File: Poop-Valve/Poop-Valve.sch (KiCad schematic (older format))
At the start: 51 parts, among them J1 RaspberryPi, J10 Valve Sig, J11 Conn_01x02_Male, J12 Relays, J13 LEDs, J14 24VDC, J15 Sensor, J16 Grove LCD, J2 Valve, J3 Charger, J4 Override, J5 Ovr Switch, J6 Power, J7 12VDC, J8 Conn_01x02_Male, J9 Conn_01x02_Male, K1 Override Relays, K2 Polarity Reverse, K3 Enable Relays, K4 Relay_Module, K5 Direction Relays, K6 Polarity Reverse, Q1 2N2222, Q2 2N2222, SW1 Override, SW2 Master Override, SW2 SW_DPDT_x2, SW3 Open/Close, U1 Opened, U2 Closed, U3 Override, U4 MCP3008

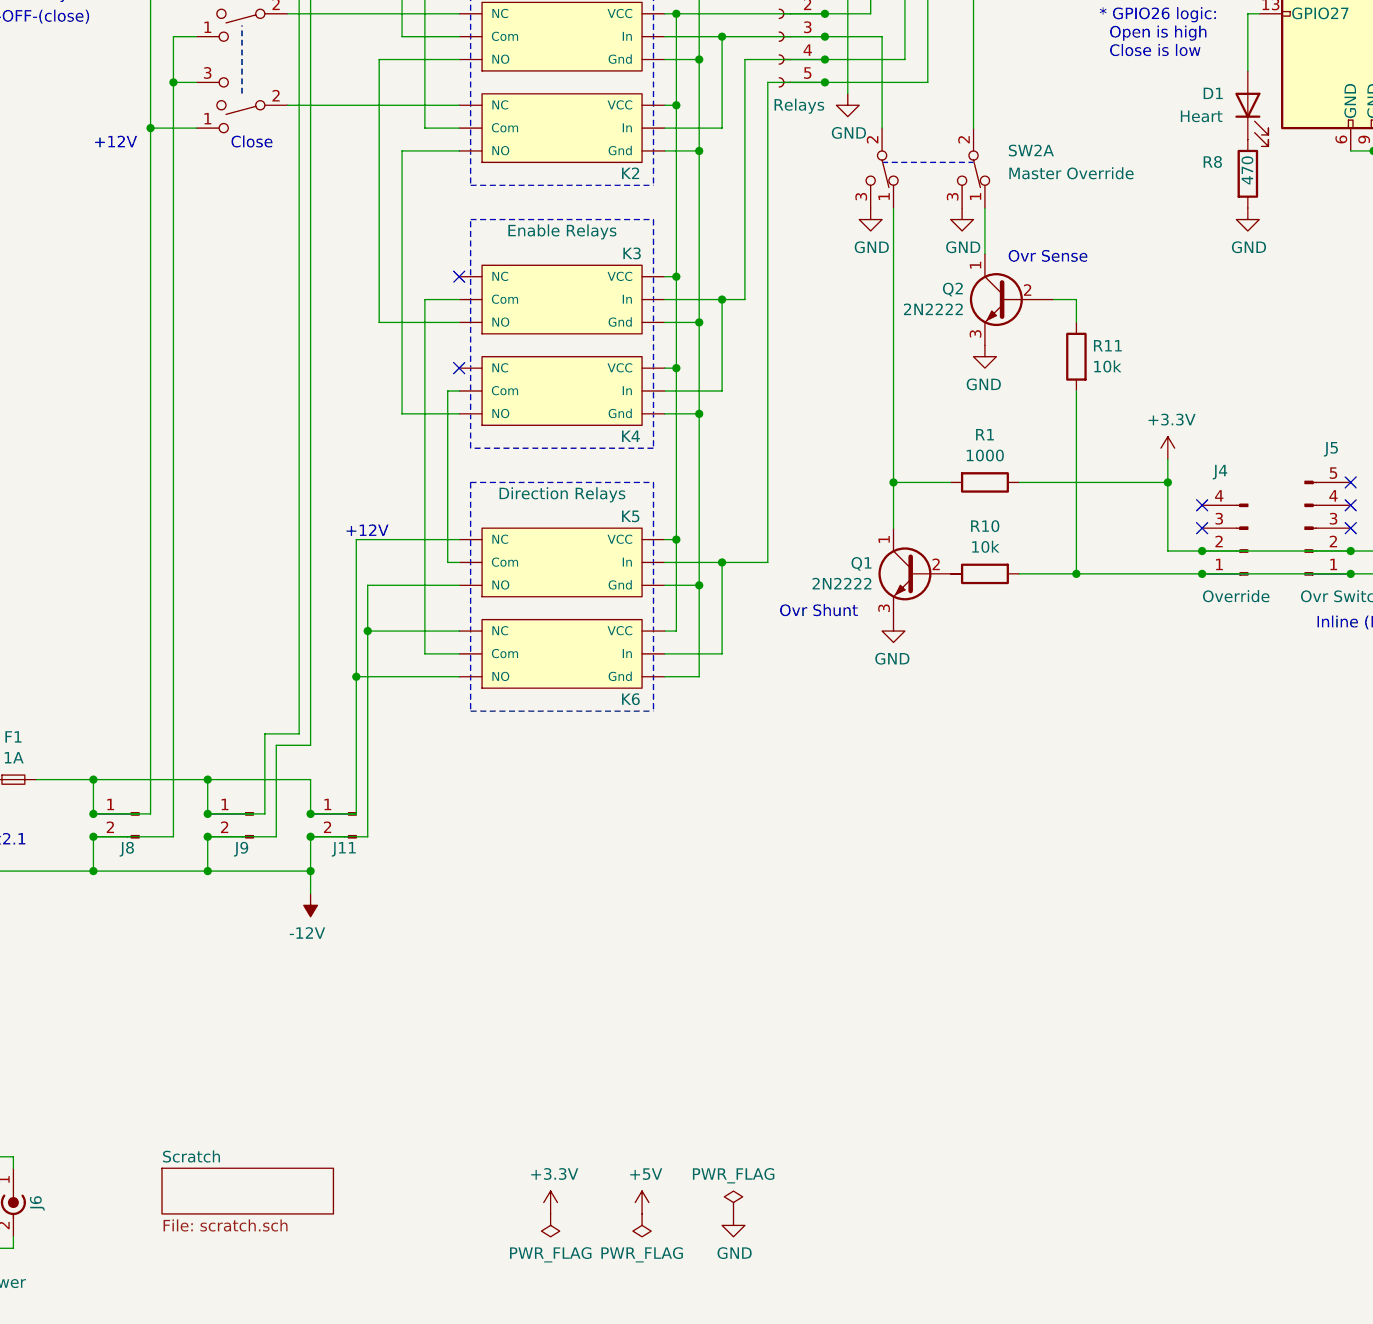
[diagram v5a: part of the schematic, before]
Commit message: v0.11 reconfigure 3.3v override relay drive
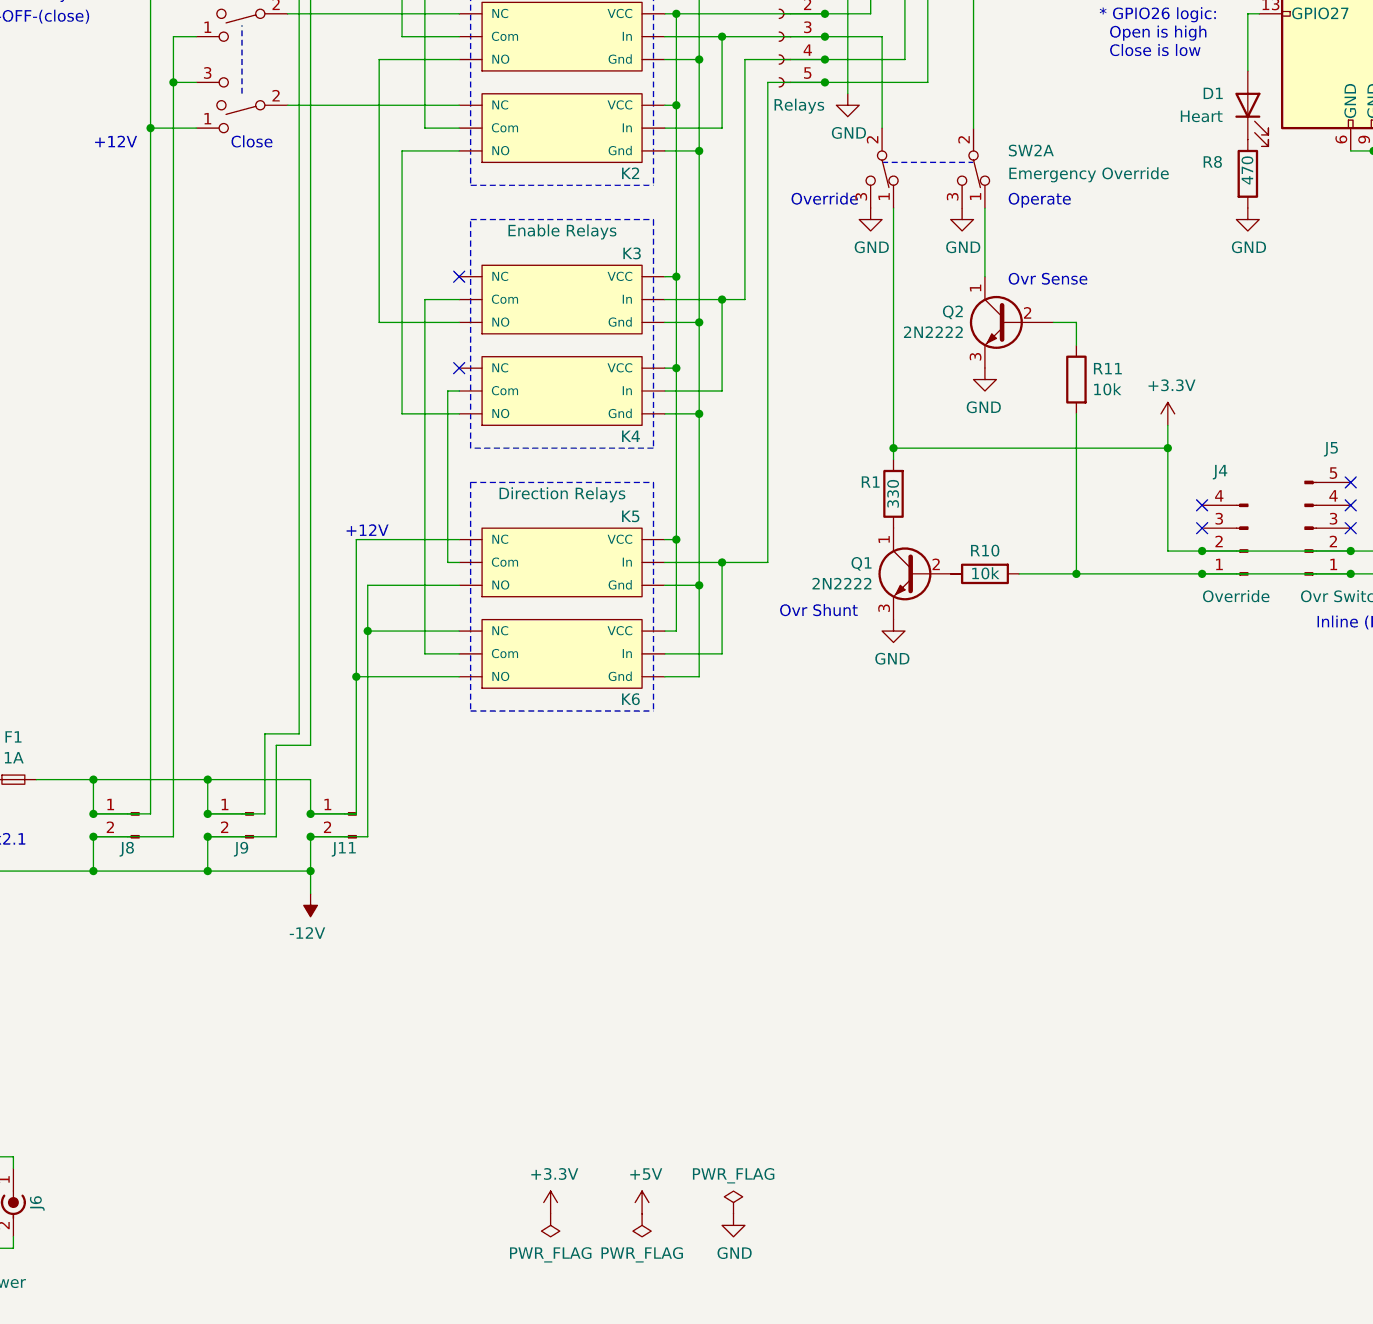
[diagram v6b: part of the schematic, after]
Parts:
- R1: value 1000 -> 330
- SW2: value Master Override -> Emergency Override
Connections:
- net +3V3: now also R1.2, SW?.1 (A); no longer R1.1
- new net: K1.~ (VCC), K2.~ (VCC), K3.~ (VCC), K4.~ (VCC), K5.~ (VCC), K6.~ (VCC)
- new net: K1.~ (VCC), K3.~ (VCC)
- new net: K3.~ (VCC), K6.~ (VCC)
- new net: K2.~ (VCC), K4.~ (VCC)
- new net: K4.~ (VCC), K5.~ (VCC)
- new net: Q1.1 (C), R1.1
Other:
- note added: "Operate"
- note added: "Override"
- moved on the sheet: Q2, R1, R11
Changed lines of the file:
@@
 $Descr USLetter 11000 8500
 encoding utf-8
-Sheet 1 2
+Sheet 1 1
 Title "Poop Valve Controller"
-Date "2023-02-01"
-Rev "0.10 (draft)"
+Date "2023-03-19"
+Rev "0.11 (draft)"
 Comp "Robert Ferguson Observatory"
-Comment1 "v0.7 correct ADC sample wiring"
-Comment2 "v0.8 reconfigure manual override; updated layout for clarity"
-Comment3 "v0.9 add override shunt and sense transistors "
-Comment4 "v0.10 add Master Override switch"
+Comment1 "v0.8 reconfigure manual override; updated layout for clarity"
+Comment2 "v0.9 add override shunt and sense transistors "
+Comment3 "v0.10 add Master Override switch"
+Comment4 "v0.11 reconfigure 3.3v override relay drive"
 $EndDescr
 $Comp
@@
 L power:+3.3V #PWR02
 U 1 1 64418208
-P 6450 5750
-F 0 "#PWR02" H 6450 5600 50  0001 C CNN
-F 1 "+3.3V" H 6465 5923 50  0000 C CNN
-F 2 "" H 6450 5750 50  0001 C CNN
-F 3 "" H 6450 5750 50  0001 C CNN
-	1    6450 5750
+P 6450 5600
+F 0 "#PWR02" H 6450 5450 50  0001 C CNN
+F 1 "+3.3V" H 6465 5773 50  0000 C CNN
+F 2 "" H 6450 5600 50  0001 C CNN
+F 3 "" H 6450 5600 50  0001 C CNN
+	1    6450 5600
 	1    0    0    -1
 $EndComp
@@
 Wire Wire Line
 	4950 3900 5200 3900
-$Sheet
-S 2050 8850 750  200
-U 65DFE627
-F0 "Scratch" 50
-F1 "scratch.sch" 50
-$EndSheet
 Wire Wire Line
 	2100 4100 2100 7400
@@
 AR Path="/65DFE627/6627A51F" Ref="R?"  Part="1"
 AR Path="/6627A51F" Ref="R10"  Part="1"
-F 0 "R10" V 5443 6250 50  0000 C CNN
-F 1 "10k" V 5534 6250 50  0000 C CNN
+F 0 "R10" V 5550 6250 50  0000 C CNN
+F 1 "10k" V 5650 6250 50  0000 C CNN
 F 2 "" V 5580 6250 50  0001 C CNN
 F 3 "~" H 5650 6250 50  0001 C CNN
@@
 	1    0    0    1
 $EndComp
-$Comp
-L Device:R R1
-U 1 1 664501BE
-P 5650 5850
-F 0 "R1" V 5443 5850 50  0000 C CNN
-F 1 "1000" V 5534 5850 50  0000 C CNN
-F 2 "" V 5580 5850 50  0001 C CNN
-F 3 "~" H 5650 5850 50  0001 C CNN
-	1    5650 5850
-	0    1    1    0
-$EndComp
 Wire Wire Line
 	5800 6250 6050 6250
-Wire Wire Line
-	6450 5750 6450 5850
 Wire Wire Line
 	6450 6150 6600 6150
 Text Notes 4750 6450 0    50   ~ 0
 Ovr Shunt
-Connection ~ 5250 5850
-Wire Wire Line
-	5250 5850 5250 6050
-Connection ~ 6450 5850
-Wire Wire Line
-	6450 5850 6450 6150
-Wire Wire Line
-	5800 5850 6450 5850
 $Comp
 L Device:R R?
 U 1 1 6659FCFC
-P 6050 5300
+P 6050 5400
 AR Path="/65DFE627/6659FCFC" Ref="R?"  Part="1"
 AR Path="/6659FCFC" Ref="R11"  Part="1"
-F 0 "R11" H 5980 5346 50  0000 R CNN
-F 1 "10k" H 5980 5255 50  0000 R CNN
-F 2 "" V 5980 5300 50  0001 C CNN
-F 3 "~" H 6050 5300 50  0001 C CNN
-	1    6050 5300
+F 0 "R11" H 5980 5446 50  0000 R CNN
+F 1 "10k" H 5980 5355 50  0000 R CNN
+F 2 "" V 5980 5400 50  0001 C CNN
+F 3 "~" H 6050 5400 50  0001 C CNN
+	1    6050 5400
 	-1   0    0    -1
 $EndComp
@@
 L power:GND #PWR?
 U 1 1 6659FD02
-P 5650 5250
+P 5650 5350
 AR Path="/65DFE627/6659FD02" Ref="#PWR?"  Part="1"
 AR Path="/6659FD02" Ref="#PWR022"  Part="1"
-F 0 "#PWR022" H 5650 5000 50  0001 C CNN
-F 1 "GND" H 5655 5077 50  0000 C CNN
-F 2 "" H 5650 5250 50  0001 C CNN
-F 3 "" H 5650 5250 50  0001 C CNN
-	1    5650 5250
+F 0 "#PWR022" H 5650 5100 50  0001 C CNN
+F 1 "GND" H 5655 5177 50  0000 C CNN
+F 2 "" H 5650 5350 50  0001 C CNN
+F 3 "" H 5650 5350 50  0001 C CNN
+	1    5650 5350
 	-1   0    0    -1
 $EndComp
@@
 	6050 6250 6600 6250
 Wire Wire Line
-	5950 5050 6050 5050
-Wire Wire Line
-	6050 5450 6050 6250
-Wire Wire Line
-	6050 5050 6050 5150
+	5950 5150 6050 5150
+Wire Wire Line
+	6050 5150 6050 5250
 Wire Wire Line
 	7800 5950 7800 6250
@@
 	4400 3700 4400 4000
 Connection ~ 4400 4000
-Text Notes 5750 4900 0    50   ~ 0
+Text Notes 5750 5000 0    50   ~ 0
 Ovr Sense
 $Comp
 L Device:Q_NPN_CBE Q?
 U 1 1 6659FCF6
-P 5750 5050
+P 5750 5150
 AR Path="/65DFE627/6659FCF6" Ref="Q?"  Part="1"
 AR Path="/6659FCF6" Ref="Q2"  Part="1"
-F 0 "Q2" H 5940 5096 50  0000 L CNN
-F 1 "2N2222" H 5940 5005 50  0000 L CNN
-F 2 "" H 5950 5150 50  0001 C CNN
-F 3 "~" H 5750 5050 50  0001 C CNN
-	1    5750 5050
-	-1   0    0    -1
-$EndComp
-Wire Wire Line
-	5650 4650 5650 4850
+F 0 "Q2" H 5940 5196 50  0000 L CNN
+F 1 "2N2222" H 5940 5105 50  0000 L CNN
+F 2 "" H 5950 5250 50  0001 C CNN
+F 3 "~" H 5750 5150 50  0001 C CNN
+	1    5750 5150
+	-1   0    0    -1
+$EndComp
 $Comp
 L Switch:SW_SPDT_SMALL SW?
@@
 $EndComp
 Wire Wire Line
-	5250 4650 5250 5850
-Wire Wire Line
-	5500 5850 5250 5850
-Wire Wire Line
 	5200 4300 5200 3900
 Wire Wire Line
@@
 P 5600 4500
 F 0 "SW2" V 5500 4650 50  0000 L CNN
-F 1 "Master Override" V 5600 4650 50  0000 L CNN
+F 1 "Emergency Override" V 5600 4650 50  0000 L CNN
 F 2 "" H 5550 4270 50  0001 C CNN
 F 3 "~" H 5550 4270 50  0001 C CNN
@@
 	0    1    1    0
 $EndComp
+Wire Wire Line
+	6050 5550 6050 6250
+Wire Wire Line
+	5650 4650 5650 4950
+Text Notes 5750 4650 0    50   ~ 0
+Operate
+Text Notes 4800 4650 0    50   ~ 0
+Override
+$Comp
+L Device:R R1
+U 1 1 664501BE
+P 5250 5900
+F 0 "R1" H 5350 5850 50  0000 C CNN
+F 1 "330" V 5250 5900 50  0000 C CNN
+F 2 "" V 5180 5900 50  0001 C CNN
+F 3 "~" H 5250 5900 50  0001 C CNN
+	1    5250 5900
+	-1   0    0    1
+$EndComp
+Wire Wire Line
+	5250 4650 5250 5700
+Wire Wire Line
+	6450 5600 6450 5700
+Wire Wire Line
+	5250 5700 6450 5700
+Connection ~ 5250 5700
+Wire Wire Line
+	5250 5700 5250 5750
+Connection ~ 6450 5700
+Wire Wire Line
+	6450 5700 6450 6150
 $EndSCHEMATC
